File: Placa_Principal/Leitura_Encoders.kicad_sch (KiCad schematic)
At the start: 0 parts

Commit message: Finalizando o esquemático e rearranjando a posição dos componentes na PCB
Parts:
- added J12, J13, J14, J15, J16, J17, J18, J19: Conn_01x02, Connector_Molex:Molex_KK-254_AE-6410-02A_1x02_P2.54mm_Vertical, symbol Connector_Generic:Conn_01x02
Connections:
- new net +5V: J12.1 (Pin_1), J14.1 (Pin_1), J16.1 (Pin_1), J18.1 (Pin_1)
- new net ESP_GPIO01: J16.2 (Pin_2)
- new net ESP_GPIO02: J17.1 (Pin_1)
- new net ESP_GPIO15: J12.2 (Pin_2)
- new net ESP_GPIO16: J13.1 (Pin_1)
- new net ESP_GPIO17: J14.2 (Pin_2)
- new net ESP_GPIO18: J15.1 (Pin_1)
- new net ESP_GPIO19: J19.1 (Pin_1)
- new net ESP_GPIO20: J18.2 (Pin_2)
- new net GND: J13.2 (Pin_2), J15.2 (Pin_2), J17.2 (Pin_2), J19.2 (Pin_2)
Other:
- note added: "Encoder Motor 1"
- note added: "Encoder Motor 2"
- note added: "Encoder Motor 3"
- note added: "Encoder Motor 4"
- company: (none) -> Titans Robotic Team
- title: (none) -> Leitura de Encoders - SSL-EL 2026

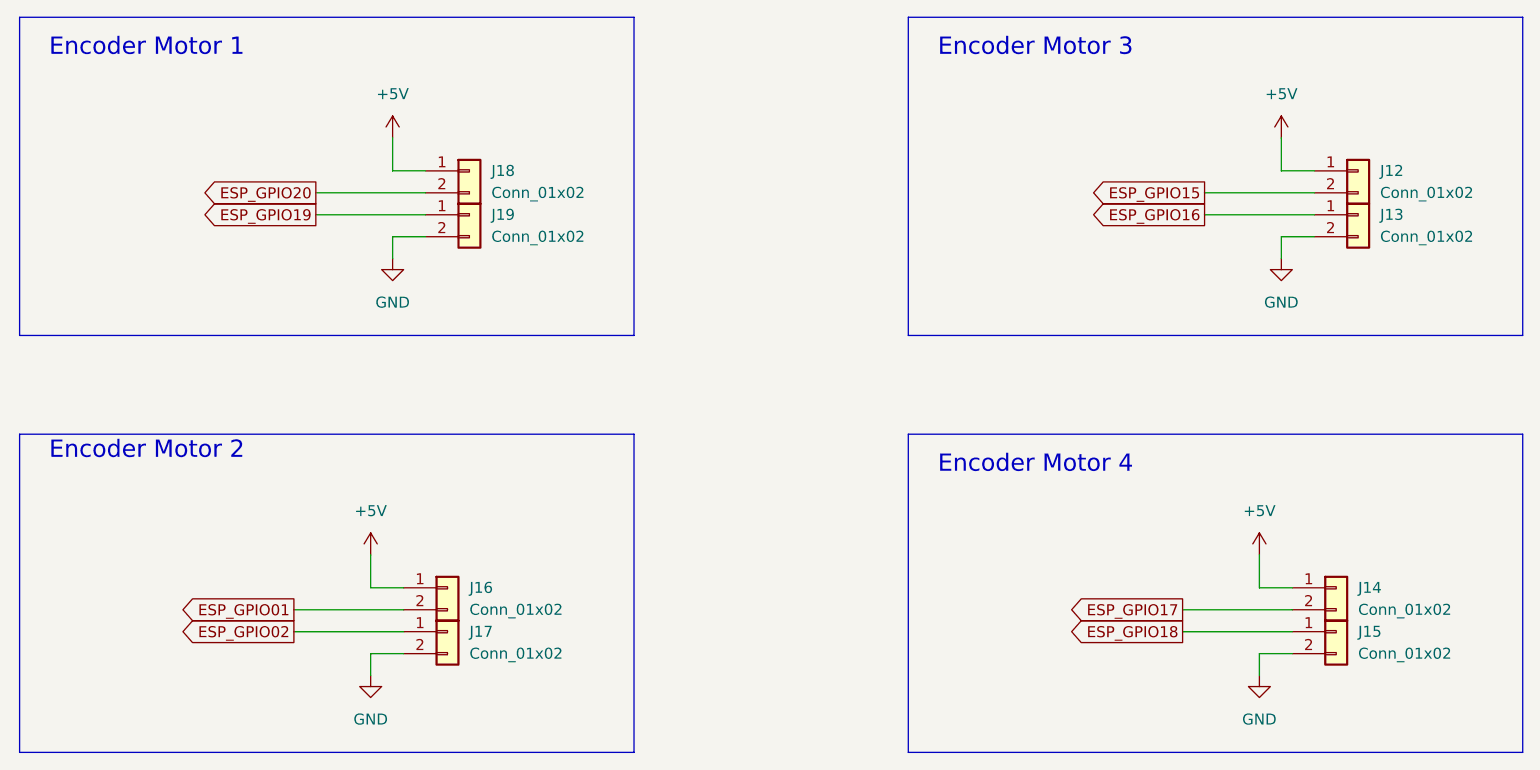
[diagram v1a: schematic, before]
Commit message: Atualizando a alimentação de todos os sensores e ESP para 3.3V e finalizando o design do monitoramento da bateria e feedback geral
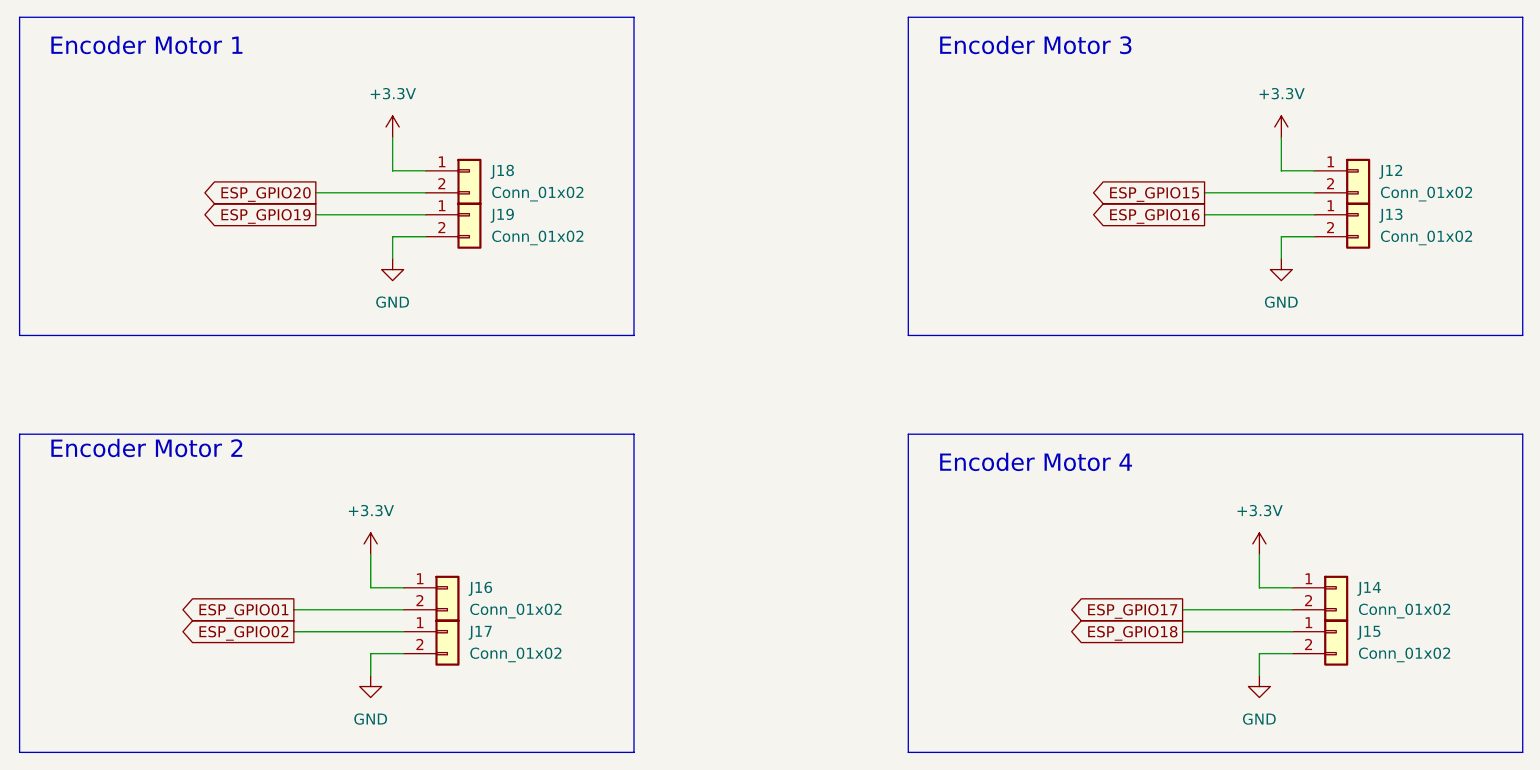
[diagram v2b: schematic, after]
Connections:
- net +5V renamed +3.3V
